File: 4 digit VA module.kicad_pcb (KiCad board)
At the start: 2 copper layers, 55 parts, among them J1 Conn_01x02, J2 Conn_01x02, J3 Conn_01x02, J4 Conn_01x03_Pin, J5 Conn_01x02_Socket, J6 Conn_01x02_Socket, Q1 BC817, Q2 BC817, Q3 BC817, Q4 BC817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

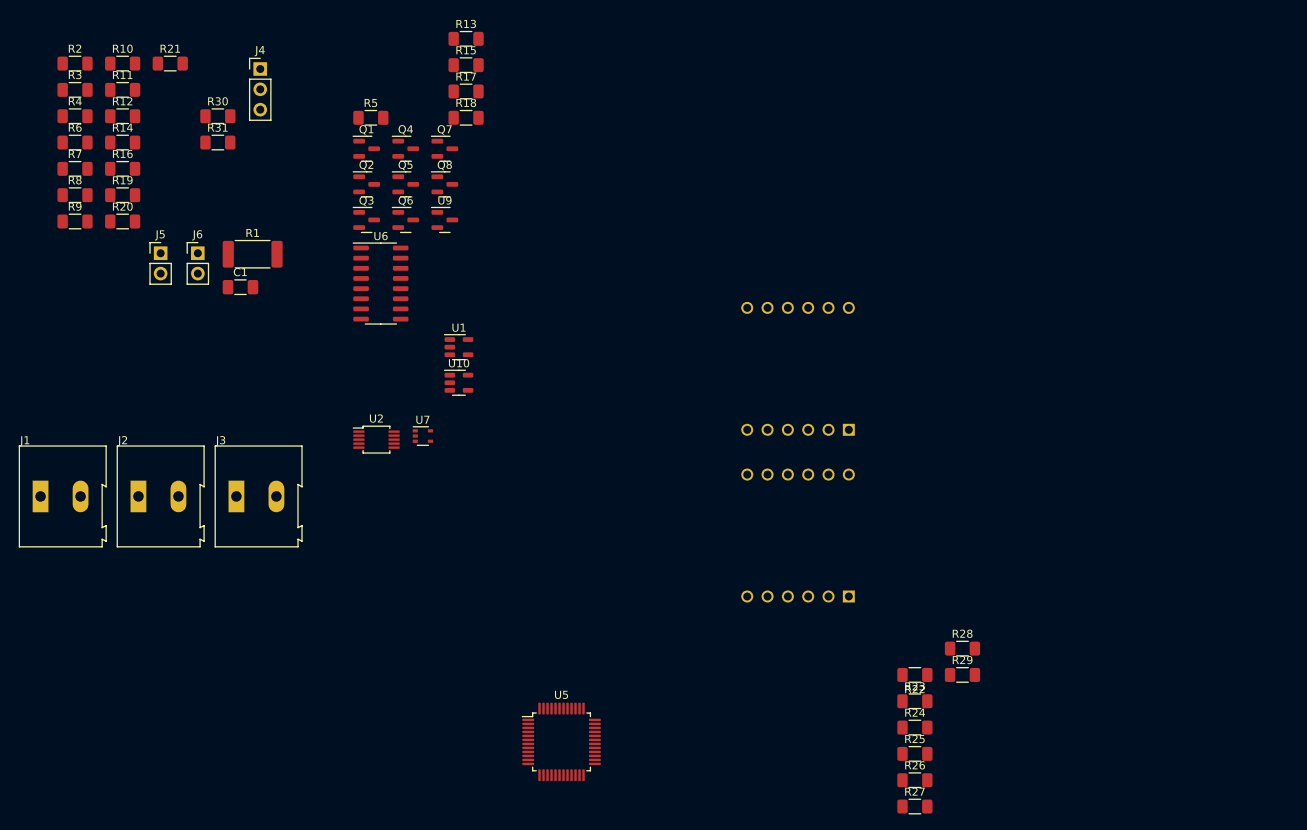
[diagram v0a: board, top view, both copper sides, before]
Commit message: Samo 7 seg je kinezijum
12 bit je malo cheapout, ukupna cena 5.8 EUR.
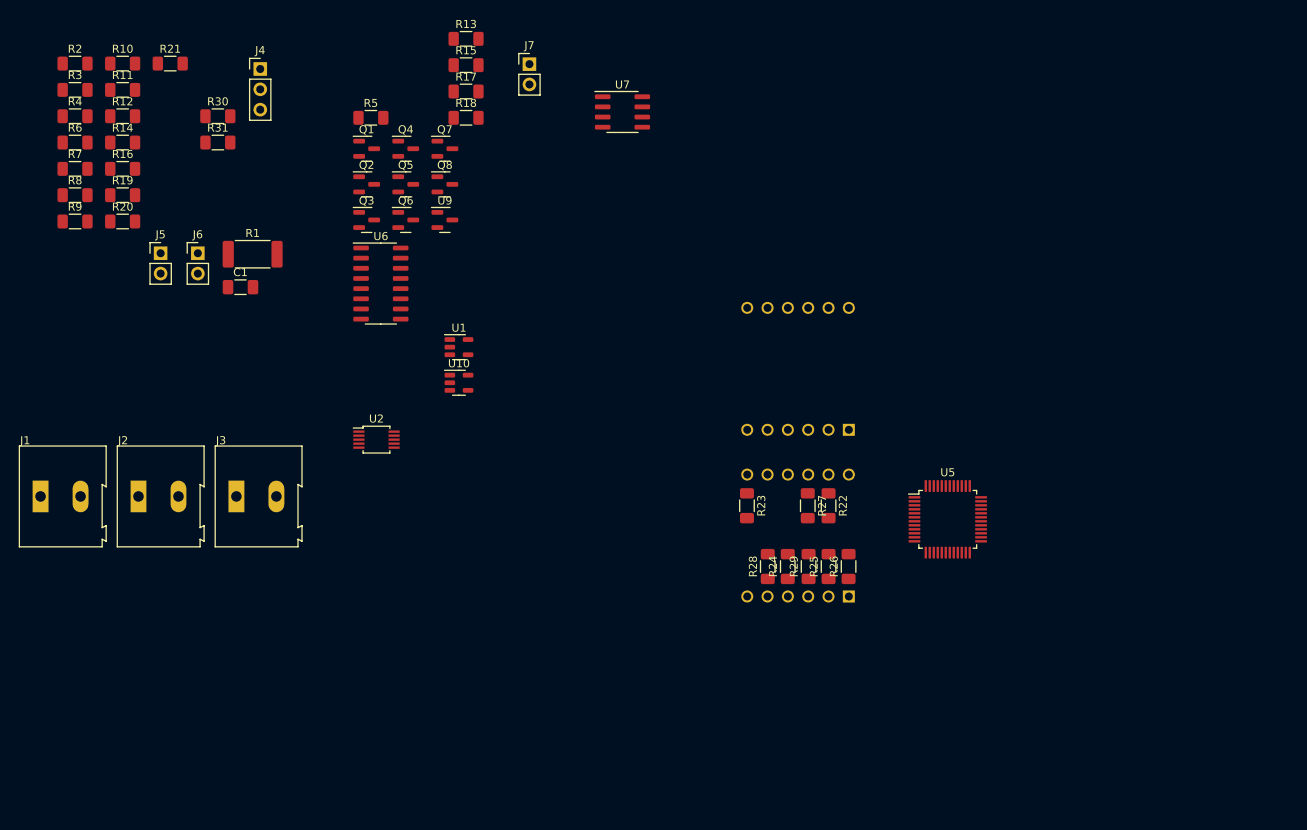
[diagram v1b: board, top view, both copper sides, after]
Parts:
- added J7: Conn_01x02_Socket, Connector_PinHeader_2.54mm:PinHeader_1x02_P2.54mm_Vertical, F.Cu at (79.8, 24.5)
- U7: footprint Package_TO_SOT_SMD:SOT-353_SC-70-5 -> Package_SO:SOIC-8_3.9x4.9mm_P1.27mm
- moved U5 55.7 mm to (132.1, 81.4)
- moved U7 47.6 mm to (91.4, 30.5)
- moved R27 39.9 mm to (114.6, 79.7), turned to -90 degrees
- moved R23 32.2 mm to (107.0, 79.7), turned to -90 degrees
- moved R26 28.0 mm to (119.7, 87.3), turned to 90 degrees
- moved R28 26.4 mm to (109.6, 87.3), turned to 90 degrees
- moved R25 25.8 mm to (117.2, 87.3), turned to 90 degrees
- moved R24 25.6 mm to (112.1, 87.3), turned to 90 degrees
- moved R22 23.7 mm to (117.2, 79.7), turned to -90 degrees
- moved R29 23.5 mm to (114.7, 87.3), turned to 90 degrees
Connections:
- U5 pad 1: unconnected-(U5-PC0-Pad1) -> SWDIO
- U5 pad 2: unconnected-(U5-PC13-Pad2) -> SWCLK
- U5 pad 21: unconnected-(U5-PB10-Pad21) -> V_IN_MUX
- U5 pad 45: unconnected-(U5-PB8-Pad45) -> VA_SEL
- U5 pad 46: unconnected-(U5-PB9-Pad46) -> V_RANGE
- U6 pad 10: unconnected-(U6-A-Pad10) -> VA_SEL
- U6 pad 9: unconnected-(U6-B-Pad9) -> V_RANGE
- U7 pad 1: V_IN_MUX -> (no net)
- U7 pad 2: 0 -> Net-(U6-X0)
- U7 pad 3: Net-(U6-X0) -> V_IN_MUX
- U7 pad 4: Net-(U6-X0) -> 0
- U7 pad 5: 3.3V -> (no net)

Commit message: Work in progress
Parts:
- removed J3: Conn_01x02, TerminalBlock:TerminalBlock_Altech_AK300-2_P5.00mm
- removed U6: SN74LV4052, Package_SO:SOIC-16_3.9x9.9mm_P1.27mm
- added U8: 74LVC1G3157, Package_TO_SOT_SMD:SOT-363_SC-70-6_Handsoldering, F.Cu at (104.1, 57.4)
- J2: value Conn_01x02 -> Conn_01x03; footprint TerminalBlock:TerminalBlock_Altech_AK300-2_P5.00mm -> Connector_JST:JST_EH_B3B-EH-A_1x03_P2.50mm_Vertical
- U3, U4: value CC56-12GWA -> 3641BS; footprint Display_7Segment:CC56-12GWA -> Pretty feet:3641; moved to F.Cu
- moved J2 65.0 mm to (92.6, 58.1)
- moved U3 63.1 mm to (99.6, 31.2), turned to 0 degrees
- moved U4 39.2 mm to (115.8, 31.2), turned to 0 degrees
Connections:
- J2 pad 1: V_in_pos -> 0
- J2 pad 2: 0 -> PSU
- J7 pad 1: SWDIO -> CAL
- J7 pad 2: SWCLK -> STATE
- R15 pad 1: LEVEL_JUDGE -> Net-(U7-+)
- R17 pad 2: LEVEL_JUDGE -> Net-(U7-+)
- U5 pad 1: SWDIO -> CAL
- U5 pad 10: LEVEL_JUDGE -> unconnected-(U5-PA0-Pad10)
- U5 pad 2: SWCLK -> STATE
- U7 pad 3: V_IN_MUX -> Net-(U7-+)

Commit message: BOM za ne kinezijum je 5.3, totalno prihvatljivo.
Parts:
- removed C1: 100n, Capacitor_SMD:C_1206_3216Metric_Pad1.33x1.80mm_HandSolder
- removed J4: Conn_01x03_Pin, Connector_PinHeader_2.54mm:PinHeader_1x03_P2.54mm_Vertical
- removed J5, J6, J7: Conn_01x02_Socket, Connector_PinHeader_2.54mm:PinHeader_1x02_P2.54mm_Vertical
- removed R10, R11, R12, R14, R16, R19, R20, R21, R22, R23, R24, R25, R26, R27, R28, R29: 220, Resistor_SMD:R_1206_3216Metric_Pad1.30x1.75mm_HandSolder
- removed R15: 24.9k, Resistor_SMD:R_1206_3216Metric_Pad1.30x1.75mm_HandSolder
- removed R17: 220k, Resistor_SMD:R_1206_3216Metric_Pad1.30x1.75mm_HandSolder
- removed R30: 4.99k, Resistor_SMD:R_1206_3216Metric_Pad1.30x1.75mm_HandSolder
- removed U7: TLV07, Package_SO:SOIC-8_3.9x4.9mm_P1.27mm
- added C2: 100n, Capacitor_SMD:C_1206_3216Metric_Pad1.33x1.80mm_HandSolder, F.Cu at (63.1, 62.4)
- added C3: 100n, Capacitor_SMD:C_1206_3216Metric_Pad1.33x1.80mm_HandSolder, F.Cu at (63.1, 65.7)
- added C4: 100n, Capacitor_SMD:C_1206_3216Metric_Pad1.33x1.80mm_HandSolder, F.Cu at (63.1, 69.1)
- added C5: 100n, Capacitor_SMD:C_1206_3216Metric_Pad1.33x1.80mm_HandSolder, F.Cu at (63.1, 72.4)
- added C6: 100n, Capacitor_SMD:C_1206_3216Metric_Pad1.33x1.80mm_HandSolder, F.Cu at (63.1, 75.8)
- added J10: Conn_01x02_Socket, Connector_PinHeader_2.54mm:PinHeader_1x02_P2.54mm_Vertical, F.Cu at (73.0, 63.0)
- added J3: Conn_01x02_Socket, Connector_PinHeader_2.54mm:PinHeader_1x02_P2.54mm_Vertical, F.Cu at (68.4, 63.0)
- added J8: Conn_01x03_Pin, Connector_PinHeader_2.54mm:PinHeader_1x03_P2.54mm_Vertical, F.Cu at (89.5, 71.6)
- added J9: Conn_01x03_Pin, Connector_PinHeader_2.54mm:PinHeader_1x03_P2.54mm_Vertical, F.Cu at (94.2, 71.6)
- added R32: 220, Resistor_SMD:R_0603_1608Metric_Pad0.98x0.95mm_HandSolder, F.Cu at (159.1, 42.1)
- added R33: 220, Resistor_SMD:R_0603_1608Metric_Pad0.98x0.95mm_HandSolder, F.Cu at (156.5, 42.0)
- added R34: 220, Resistor_SMD:R_0603_1608Metric_Pad0.98x0.95mm_HandSolder, F.Cu at (153.7, 39.6)
- added R35: 220, Resistor_SMD:R_0603_1608Metric_Pad0.98x0.95mm_HandSolder, F.Cu at (156.3, 39.9)
- added R36: 220, Resistor_SMD:R_0603_1608Metric_Pad0.98x0.95mm_HandSolder, F.Cu at (151.4, 42.2)
- added R37: 220, Resistor_SMD:R_0603_1608Metric_Pad0.98x0.95mm_HandSolder, F.Cu at (148.7, 42.0)
- added R38: 220, Resistor_SMD:R_0603_1608Metric_Pad0.98x0.95mm_HandSolder, F.Cu at (146.1, 39.9)
- added R39: 220, Resistor_SMD:R_0603_1608Metric_Pad0.98x0.95mm_HandSolder, F.Cu at (153.5, 42.2)
- added U6: STM32L010C6Tx, Package_QFP:LQFP-48_7x7mm_P0.5mm, F.Cu at (167.7, 45.6)
- R13, R2, R3, R4, R5, R6, R7, R8, R9: footprint Resistor_SMD:R_1206_3216Metric_Pad1.30x1.75mm_HandSolder -> Resistor_SMD:R_0603_1608Metric_Pad0.98x0.95mm_HandSolder
- R18: value 750k -> 1Meg; footprint Resistor_SMD:R_1206_3216Metric_Pad1.30x1.75mm_HandSolder -> Resistor_SMD:R_0603_1608Metric_Pad0.98x0.95mm_HandSolder
- R31: value 100 -> 25.64k; footprint Resistor_SMD:R_1206_3216Metric_Pad1.30x1.75mm_HandSolder -> Resistor_SMD:R_0603_1608Metric_Pad0.98x0.95mm_HandSolder
- U3, U4: value 3641BS -> 2841BS; footprint Pretty feet:3641 -> Pretty feet:2841; moved to B.Cu
- U5: value STM32L010C6Tx -> LM321; footprint Package_QFP:LQFP-48_7x7mm_P0.5mm -> Package_TO_SOT_SMD:SOT-23-5
- moved R2 146.4 mm to (168.7, 38.8), turned to -90 degrees
- moved R3 144.6 mm to (167.2, 38.8), turned to -90 degrees
- moved R4 118.0 mm to (140.6, 40.5), turned to 90 degrees
- moved U2 111.8 mm to (171.0, 53.0), turned to 180 degrees
- moved R5 110.5 mm to (170.2, 38.8), turned to -90 degrees
- moved Q3 102.5 mm to (161.9, 40.5), turned to -90 degrees
- moved Q4 97.6 mm to (161.9, 36.5), turned to -90 degrees
- moved Q1 84.0 mm to (142.9, 44.6), turned to -90 degrees
- moved Q2 83.8 mm to (143.2, 36.3)
- moved U3 64.1 mm to (158.8, 55.8), turned to 90 degrees
- moved U5 61.0 mm to (72.0, 71.3)
- moved R31 57.4 mm to (96.7, 47.7)
- moved R6 56.8 mm to (78.8, 44.4)
- moved R7 56.8 mm to (78.8, 47.7)
- moved R8 56.8 mm to (78.8, 51.0)
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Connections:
- R18 pad 2: Net-(R18-Pad2) -> Net-(U5-+)
- R31 pad 1: Net-(R15-Pad2) -> Net-(U5-+)
- U3 pad 1: Net-(U3-e) -> E
- U3 pad 10: Net-(U3-f) -> F
- U3 pad 11: Net-(U3-a) -> A
- U3 pad 12: Net-(Q4-C) -> Net-(Q8-C)
- U3 pad 2: Net-(U3-d) -> D
- U3 pad 3: Net-(U3-DPX) -> DP
- U3 pad 4: Net-(U3-c) -> C
- U3 pad 5: Net-(U3-g) -> G
- U3 pad 6: Net-(Q1-C) -> Net-(Q5-C)
- U3 pad 7: Net-(U3-b) -> B
- U3 pad 8: Net-(Q2-C) -> Net-(Q6-C)
- U3 pad 9: Net-(Q3-C) -> Net-(Q7-C)
- U4 pad 1: Net-(U4-e) -> E
- U4 pad 10: Net-(U4-f) -> F
- U4 pad 11: Net-(U4-a) -> A
- U4 pad 12: Net-(Q8-C) -> Net-(Q4-C)
- U4 pad 2: Net-(U4-d) -> D
- U4 pad 3: Net-(U4-DPX) -> DP
- U4 pad 4: Net-(U4-c) -> C
- U4 pad 5: Net-(U4-g) -> G
- U4 pad 6: Net-(Q5-C) -> Net-(Q1-C)
- U4 pad 7: Net-(U4-b) -> B
- U4 pad 8: Net-(Q6-C) -> Net-(Q2-C)
- U4 pad 9: Net-(Q7-C) -> Net-(Q3-C)
- U5 pad 1: CAL -> Net-(U5-+)
- U5 pad 2: STATE -> 0
- U5 pad 3: unconnected-(U5-PC14-Pad3) -> Net-(U5--)
- U5 pad 4: unconnected-(U5-PC15-Pad4) -> Net-(U5--)
- U5 pad 5: unconnected-(U5-PH0-Pad5) -> 3.3V
- U8 pad 3: Net-(U7--) -> Net-(U5--)
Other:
- board outline added: 44 x 24 mm
- copper layers 2 -> 4

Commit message: WIP
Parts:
- removed J10: Conn_01x02_Socket, Connector_PinHeader_2.54mm:PinHeader_1x02_P2.54mm_Vertical
- removed J8: Conn_01x03_Pin, Connector_PinHeader_2.54mm:PinHeader_1x03_P2.54mm_Vertical
- removed U10: AP2112K-3.3, Package_TO_SOT_SMD:SOT-23-5
- added C1: 1u, Capacitor_SMD:C_0603_1608Metric_Pad1.08x0.95mm_HandSolder, B.Cu at (142.3, 50.6)
- added C10: 100n, Capacitor_SMD:C_0603_1608Metric_Pad1.08x0.95mm_HandSolder, F.Cu at (161.3, 51.5)
- added C11: 100n, Capacitor_SMD:C_0603_1608Metric_Pad1.08x0.95mm_HandSolder, F.Cu at (158.9, 42.2)
- added C12: 100n, Capacitor_SMD:C_0603_1608Metric_Pad1.08x0.95mm_HandSolder, F.Cu at (172.8, 45.0)
- added C7: 1u, Capacitor_SMD:C_0603_1608Metric_Pad1.08x0.95mm_HandSolder, B.Cu at (141.7, 46.3)
- added C8: 1u, Capacitor_SMD:C_0603_1608Metric_Pad1.08x0.95mm_HandSolder, B.Cu at (140.2, 46.3)
- added C9: 100p, Capacitor_SMD:C_0603_1608Metric_Pad1.08x0.95mm_HandSolder, B.Cu at (138.7, 46.3)
- added U7: AP2210K-3.3TRG1, Package_TO_SOT_SMD:SOT-23-5, B.Cu at (139.6, 50.3)
- C2, C5, C6: footprint Capacitor_SMD:C_1206_3216Metric_Pad1.33x1.80mm_HandSolder -> Capacitor_SMD:C_0603_1608Metric_Pad1.08x0.95mm_HandSolder
- C3, C4: footprint Capacitor_SMD:C_1206_3216Metric_Pad1.33x1.80mm_HandSolder -> Capacitor_SMD:C_0603_1608Metric_Pad1.08x0.95mm_HandSolder; moved to B.Cu
- R1: value 50m -> 10m
- R13: value 900k -> 1k
- U1: moved to B.Cu
- moved C6 114.1 mm to (173.7, 48.0), turned to 90 degrees
- moved C5 111.3 mm to (172.8, 53.8), turned to 180 degrees
- moved C2 111.2 mm to (173.7, 51.3), turned to 90 degrees
- moved C3 109.3 mm to (168.6, 37.2)
- moved C4 105.2 mm to (163.2, 36.8)
- moved U5 105.0 mm to (172.7, 41.8), turned to 90 degrees
- moved J3 102.1 mm to (170.3, 56.6), turned to 90 degrees
- moved J1 91.6 mm to (134.6, 41.4)
- moved J2 90.3 mm to (134.5, 54.9)
- moved U9 89.9 mm to (172.5, 36.2)
- moved R13 87.6 mm to (172.4, 38.6), turned to 180 degrees
- moved U8 87.2 mm to (165.4, 36.8), turned to 90 degrees
- moved R9 83.2 mm to (162.1, 54.0)
- moved R8 79.0 mm to (157.8, 54.0)
- moved R7 75.9 mm to (154.5, 54.0)
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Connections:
- J9 pad 2: SWCLK -> SWDIO
- J9 pad 3: SWDIO -> SWCLK
- R2 pad 2: CC2 -> CC6
- R3 pad 2: CC3 -> CC7
- R4 pad 2: CC4 -> CC8
- R5 pad 2: CC1 -> CC5
- R6 pad 2: CC8 -> CC4
- R7 pad 2: CC7 -> CC3
- R8 pad 2: CC6 -> CC2
- R9 pad 2: CC5 -> CC1
- U6 pad 12: USART_TX -> unconnected-(U6-PA2-Pad12)
- U6 pad 13: USART_RX -> unconnected-(U6-PA3-Pad13)
- U6 pad 42: VA_SEL -> CC4
- U6 pad 44: Net-(J8-Pin_2) -> unconnected-(U6-BOOT0-Pad44)
- U6 pad 46: CC4 -> VA_SEL
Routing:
- net 3.3V: track 0.00 -> 41.5 mm, vias 0 -> 6
- net I_OUT: track 0.00 -> 38.9 mm, vias 0 -> 1
- net Net-(U6-PA11): track 0.00 -> 29.4 mm, vias 0 -> 2
- net Net-(U6-PA10): track 0.00 -> 25.5 mm
- net CC4: track 0.00 -> 25.1 mm, vias 0 -> 2
- net VA_SEL: track 0.00 -> 24.8 mm, vias 0 -> 2
- net Net-(Q1-B): track 0.00 -> 23.7 mm, vias 0 -> 2
- net Net-(U6-PA12): track 0.00 -> 23.5 mm, vias 0 -> 2
- net CC3: track 0.00 -> 23.2 mm, vias 0 -> 2
- net Net-(U6-PB12): track 0.00 -> 22.2 mm, vias 0 -> 2
- net Net-(U6-PA9): track 0.00 -> 18.6 mm
- net Net-(Q2-B): track 0.00 -> 16.1 mm
- net D: track 0.00 -> 14.9 mm
- net E: track 0.00 -> 14.8 mm
- net A: track 0.00 -> 14.5 mm
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
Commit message: Izgleda kao da je PCB gotov, treba proveriti dimenziju.
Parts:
- added REF**: OSHW-Logo2_7.3x6mm_SilkScreen, Symbol:OSHW-Logo2_7.3x6mm_SilkScreen, B.Cu at (163.6, 43.2)
- moved C11 14.1 mm to (172.7, 45.0), turned to 180 degrees
- moved C12 13.3 mm to (161.4, 51.8), turned to -90 degrees
- moved C10 9.06 mm to (157.9, 43.1), turned to 0 degrees
- moved R33 2.12 mm to (157.9, 41.6)
- moved R32 0.69 mm to (161.5, 46.2)
- moved C5 0.42 mm to (172.7, 54.2)
- moved R9 0.29 mm to (162.3, 54.2)
- moved U3 0.06 mm to (158.9, 55.8)
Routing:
- net Net-(U5-+): track 1.72 -> 34.2 mm, vias 0 -> 2
- net 0: track 0.39 -> 15.9 mm, vias 7 -> 21
- net current_in_pos: track 14.2 -> 4.79 mm
- net current_in_neg: track 10.8 -> 1.81 mm
- net PSU: track 6.97 -> 12.8 mm
- net CC3: track 23.2 -> 19.0 mm
- net D: track 14.9 -> 17.2 mm
- net Net-(U6-PB11): track 10.8 -> 9.25 mm
- net 3.3V: track 41.5 -> 40.7 mm, vias 6 -> 9
- net CC4: track 25.1 -> 25.9 mm
- net Net-(Q3-B): track 11.9 -> 11.3 mm
- added copper zone on B.Cu, net 0
- added copper zone on In2.Cu, net 3.3V
- added copper zone on F.Cu, net current_in_neg
- added copper zone on F.Cu, net current_in_pos
